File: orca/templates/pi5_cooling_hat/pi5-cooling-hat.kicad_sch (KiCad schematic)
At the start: 15 parts, among them J1 Raspberry Pi 5 GPIO, J2 5V 4-wire PWM fan, Q1 2N7002K

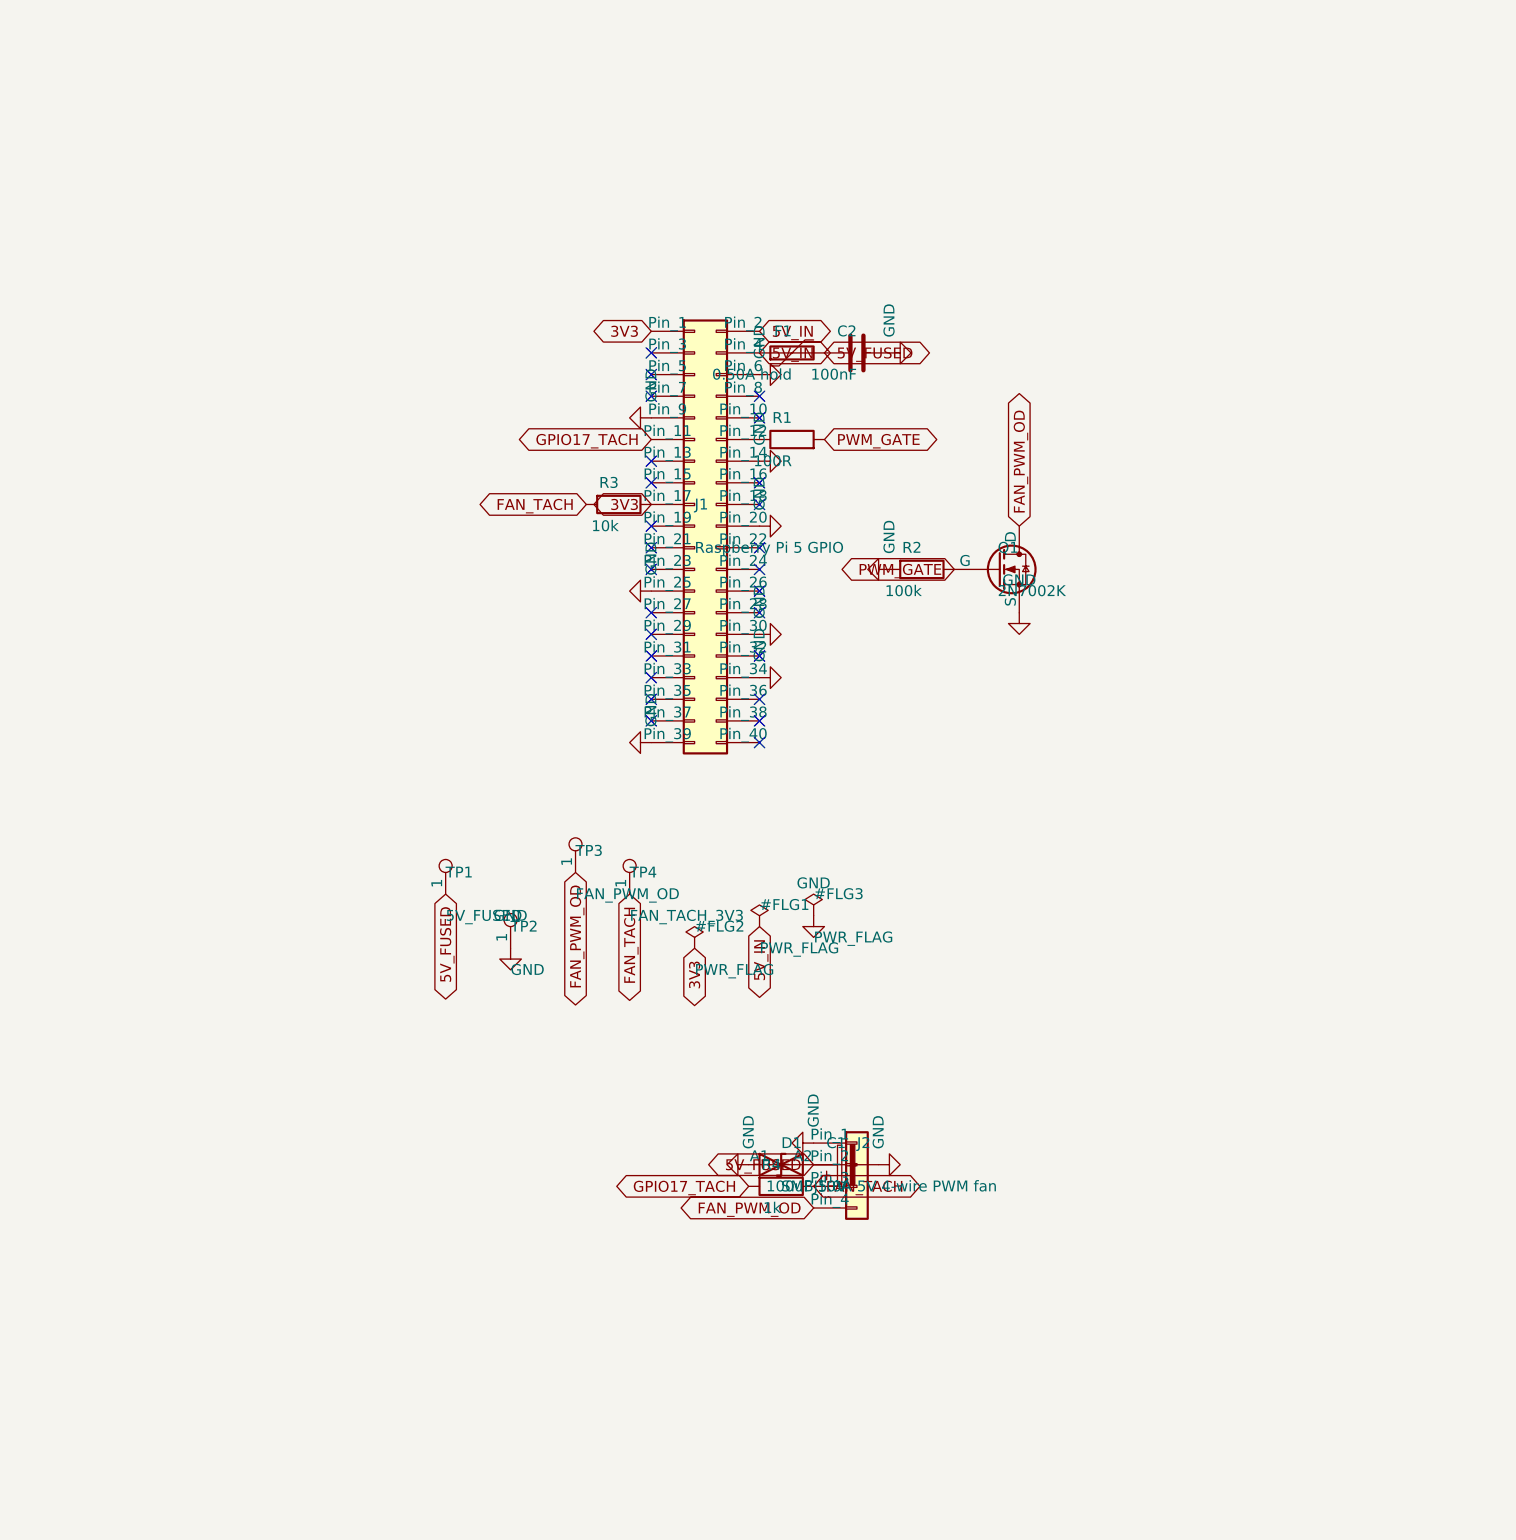
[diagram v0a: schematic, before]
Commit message: Add free engineering review panel and repair Pi HAT design
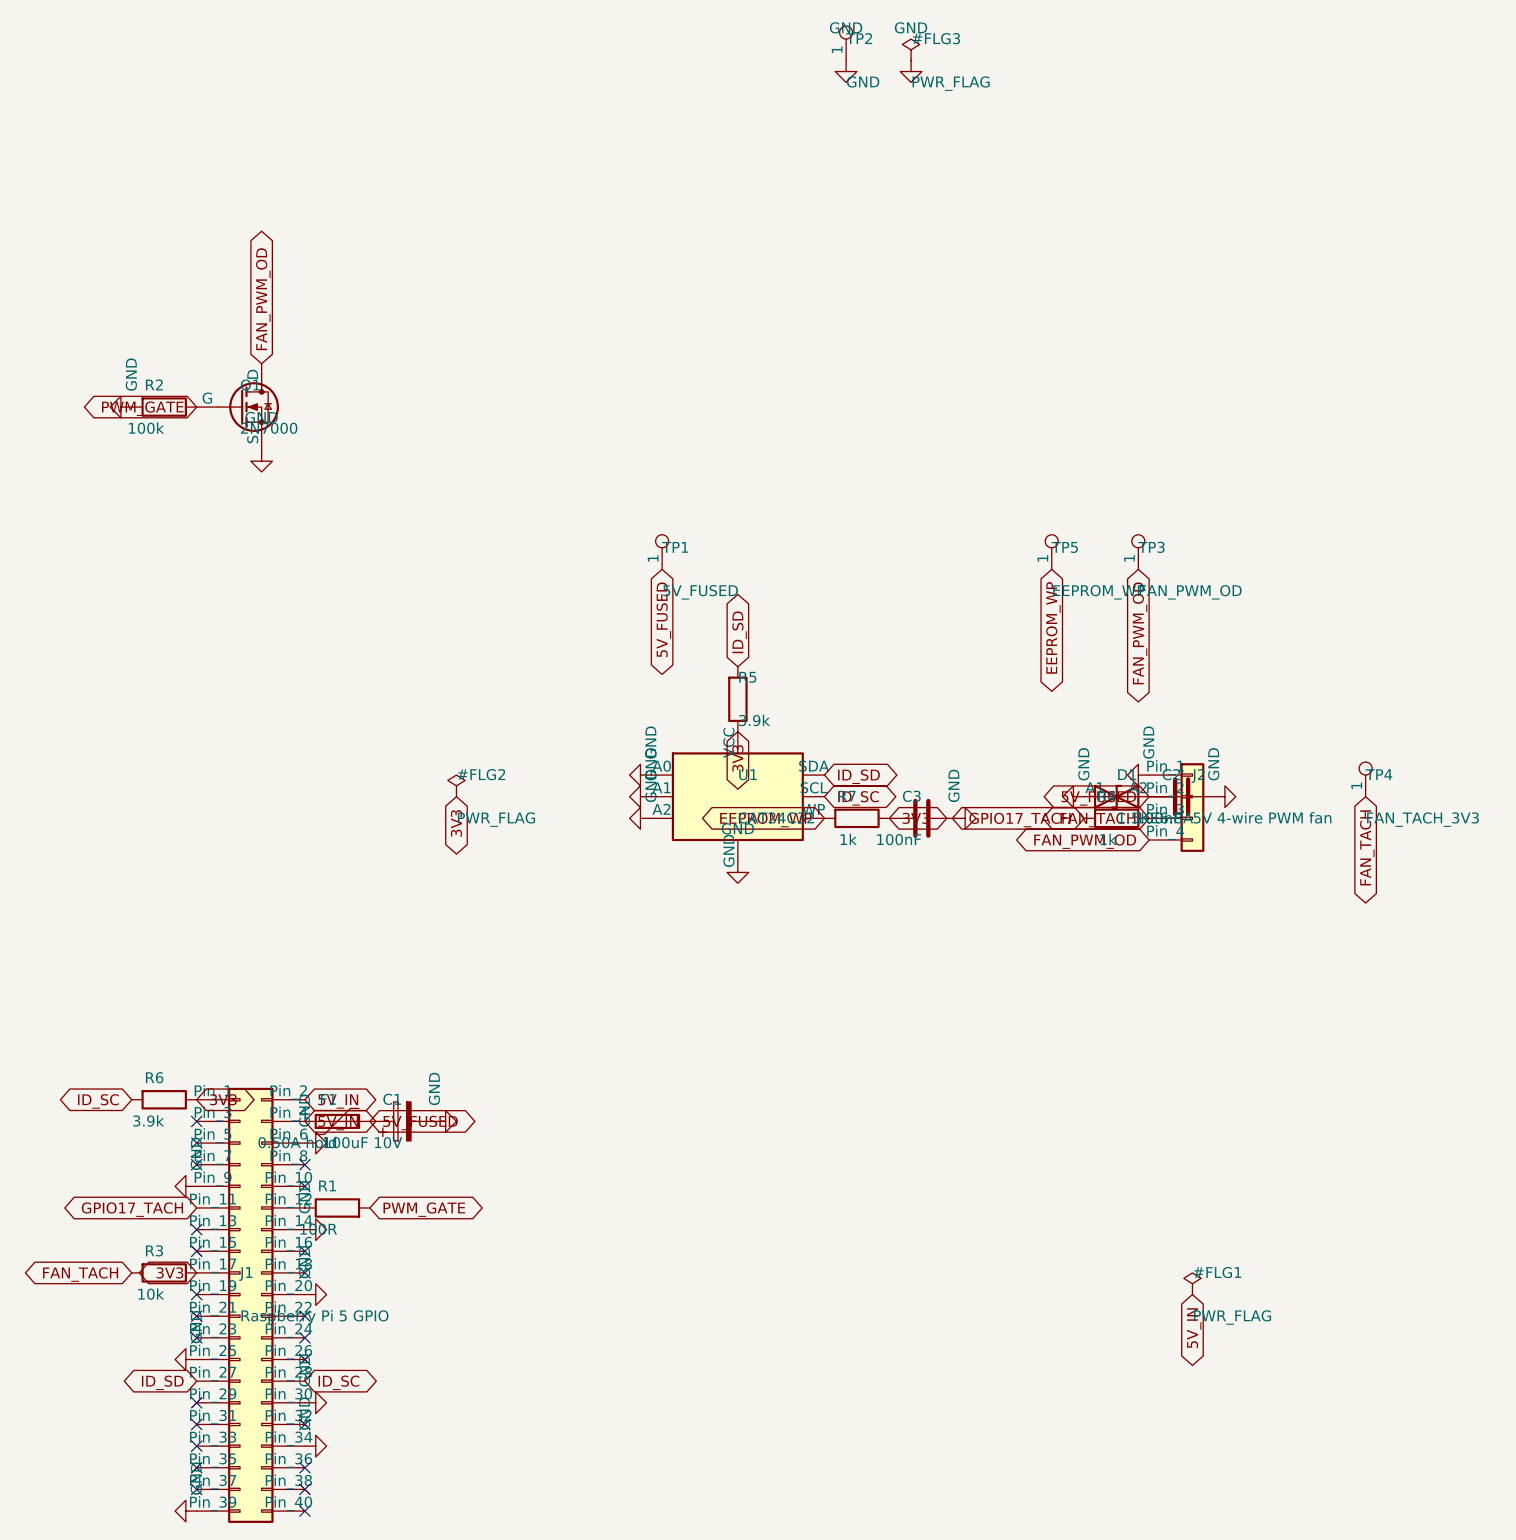
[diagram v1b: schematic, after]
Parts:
- added C3: 100nF, Capacitor_THT:C_Disc_D5.0mm_W2.5mm_P5.00mm, symbol Device:C
- added R5, R6: 3.9k, Resistor_THT:R_Axial_DIN0207_L6.3mm_D2.5mm_P10.16mm_Horizontal, symbol Device:R
- added R7: 1k, Resistor_THT:R_Axial_DIN0207_L6.3mm_D2.5mm_P10.16mm_Horizontal, symbol Device:R
- added TP5: EEPROM_WP, TestPoint:TestPoint_Plated_Hole_D2.0mm, symbol Connector:TestPoint
- added U1: CAT24C32, Package_DIP:DIP-8_W7.62mm, symbol Memory_EEPROM:24LC32
- C1: footprint Capacitor_SMD:CP_Elec_6.3x5.8 -> Capacitor_THT:CP_Radial_D6.3mm_P2.50mm
- C2: footprint Capacitor_SMD:C_0603_1608Metric -> Capacitor_THT:C_Disc_D5.0mm_W2.5mm_P5.00mm
- D1: value SMBJ5.0A -> 1.5KE6.8A; footprint Diode_SMD:D_SMB -> Diode_THT:D_DO-15_P10.16mm_Horizontal
- Q1: value 2N7002K -> 2N7000; footprint Package_TO_SOT_SMD:SOT-23 -> Package_TO_SOT_THT:TO-92_Inline
- R1, R2, R3, R4: footprint Resistor_SMD:R_0603_1608Metric -> Resistor_THT:R_Axial_DIN0207_L6.3mm_D2.5mm_P10.16mm_Horizontal
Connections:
- net 3V3: now also C3.1, R5.1, R6.1, R7.1, U1.8 (VCC)
- net GND: now also C3.2, U1.1 (A0), U1.2 (A1), U1.3 (A2), U1.4 (GND)
- net ID_SD: now reaches J1.27 (Pin_27)
- net ID_SD: now also R5.2, U1.5 (SDA)
- net ID_SC: now reaches J1.28 (Pin_28)
- net ID_SC: now also R6.2, U1.6 (SCL)
- new net EEPROM_WP: R7.2, TP5.1, U1.7 (WP)
- no-connect marks 26 -> 24
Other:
- moved on the sheet: C1, C2, D1, F1, J1, J2, Q1, R1, R2, R3, R4, TP1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
